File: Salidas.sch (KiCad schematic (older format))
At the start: 58 parts, among them J1 TB_1X2-PonchoPLC-rescue, J2 TB_1X3-PonchoPLC-rescue, J3 TB_1X2, J4 TB_1X2, J5 TB_1X2, J6 TB_1X2, Q1 FQT13N06L, Q2 FQT13N06L, Q3 FQT13N06L, Q4 FQT13N06L, U1 MCP1416, U2 MCP1416, U3 MCP1416, U4 MCP1416, U5 VO14642AABTR, U6 VO14642AABTR, U7 VO14642AABTR, U8 VO14642AABTR

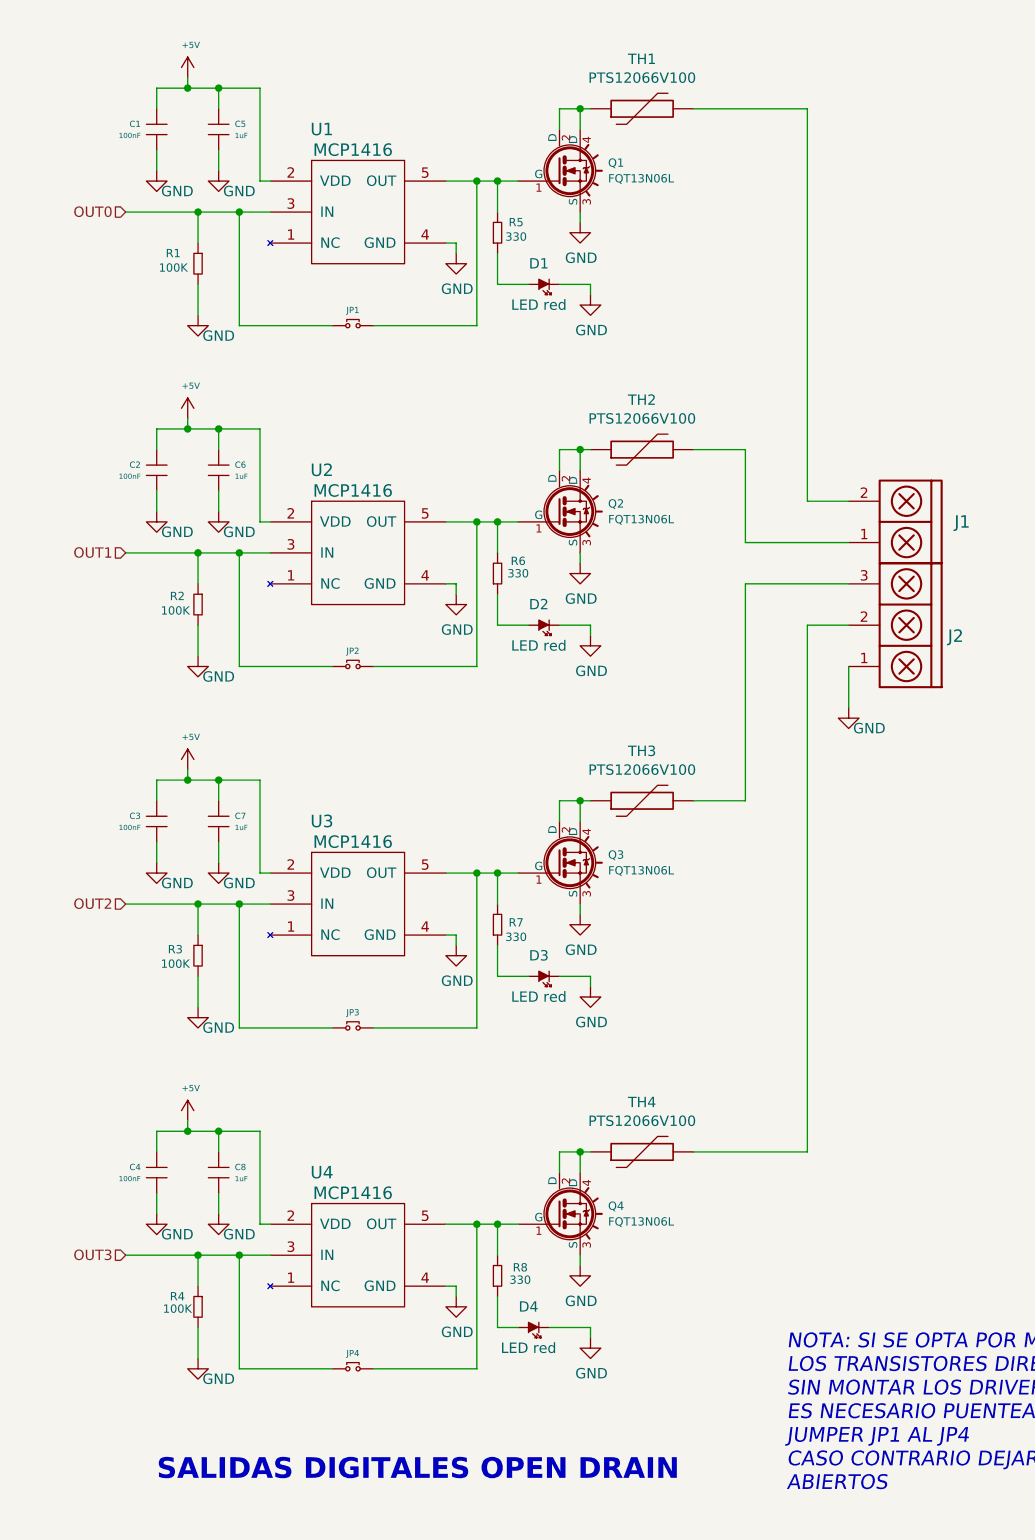
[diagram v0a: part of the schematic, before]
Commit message: Ruteo Casi terminado (faltan planos de masa)
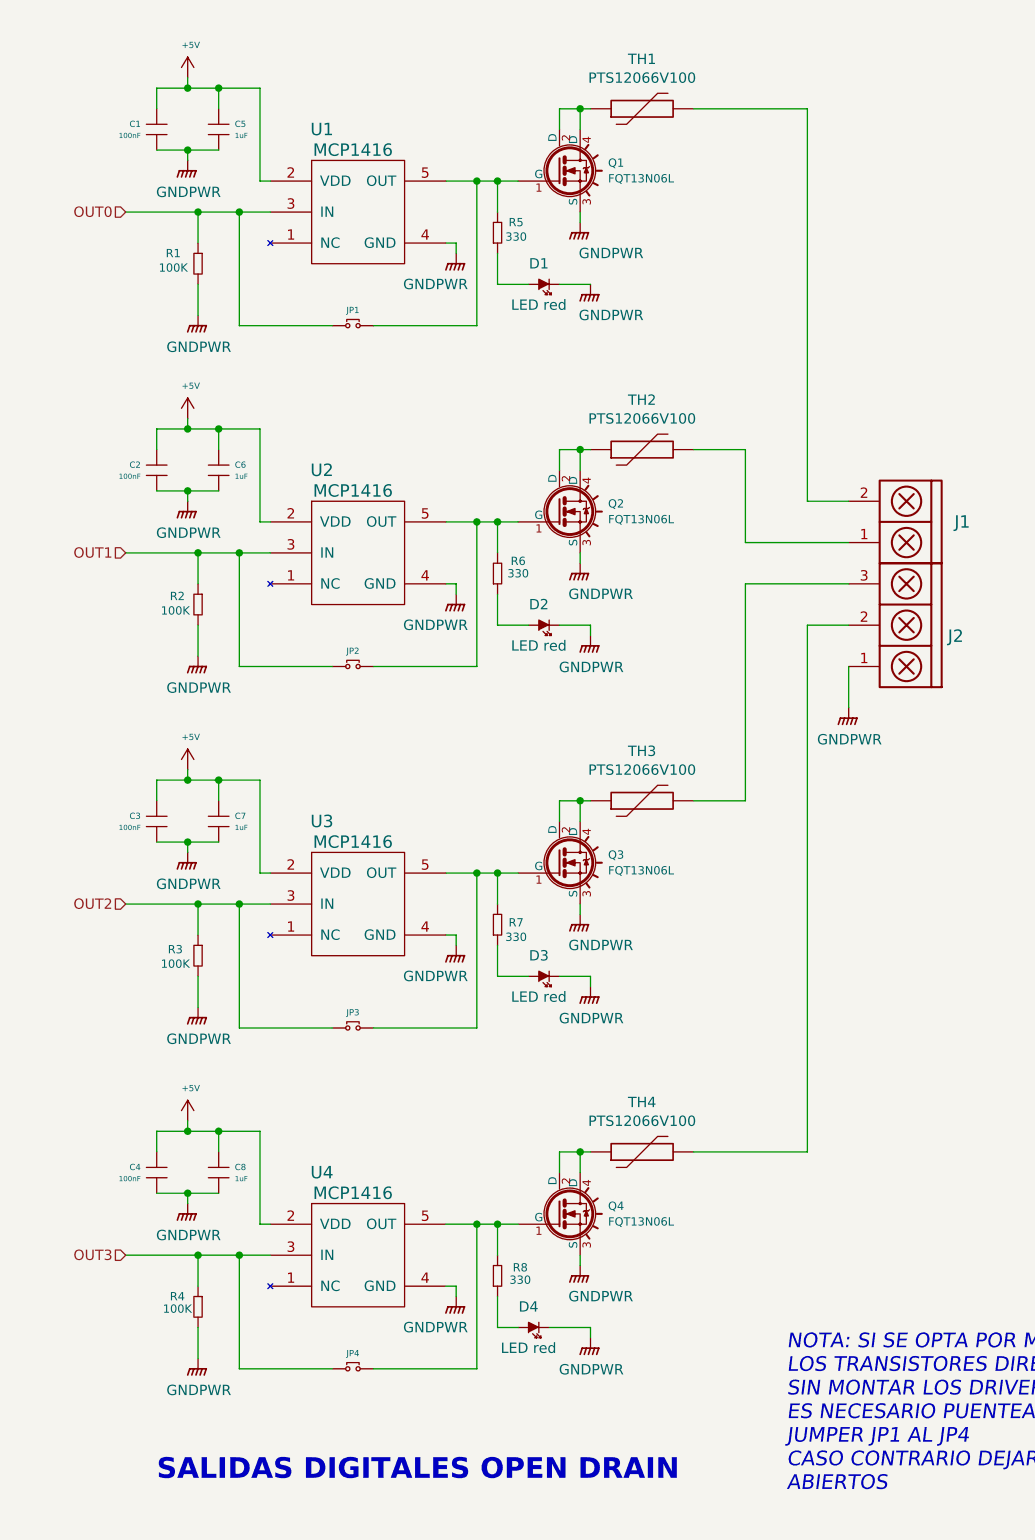
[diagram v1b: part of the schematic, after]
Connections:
- net GND: no longer C1.1 (A), C2.1 (A), C3.1 (A), C4.1 (A), C5.1 (A), C6.1 (A), C7.1 (A), C8.1 (A), D1.2 (K), D2.2 (K), D3.2 (K), D4.2 (K), J2.1, Q1.3 (S), Q2.3 (S), Q3.3 (S), Q4.3 (S), R1.2, R2.2, R3.2, R4.2, U1.4 (GND), U2.4 (GND), U3.4 (GND), U4.4 (GND)
- new net GNDPWR: C1.1 (A), C2.1 (A), C3.1 (A), C4.1 (A), C5.1 (A), C6.1 (A), C7.1 (A), C8.1 (A), D1.2 (K), D2.2 (K), D3.2 (K), D4.2 (K), J2.1, Q1.3 (S), Q2.3 (S), Q3.3 (S), Q4.3 (S), R1.2, R2.2, R3.2, R4.2, U1.4 (GND), U2.4 (GND), U3.4 (GND), U4.4 (GND)
